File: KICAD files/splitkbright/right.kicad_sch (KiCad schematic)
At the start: 83 parts, among them SW31 SW_Push, SW32 SW_Push, SW37 SW_Push, SW38 SW_Push, SW39 SW_Push, SW40 SW_Push, SW41 SW_Push, SW42 SW_Push, SW43 SW_Push, SW44 SW_Push, SW45 SW_Push, SW46 SW_Push, SW47 SW_Push, SW48 SW_Push, SW49 SW_Push, SW50 SW_Push, SW51 SW_Push, SW52 SW_Push, SW53 SW_Push, SW54 SW_Push, SW55 SW_Push, SW56 SW_Push, SW57 SW_Push, SW58 SW_Push, SW59 SW_Push, SW60 SW_Push, SW61 SW_Push, SW62 SW_Push, SW63 SW_Push, SW64 SW_Push, SW65 SW_Push, SW66 SW_Push, SW67 SW_Push, SW68 SW_Push, SW69 SW_Push, SW70 SW_Push, SW71 SW_Push, SW72 SW_Push, SW73 SW_Push, SW74 SW_Push, U1 nice_nano

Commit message: Edited PCBs
- Added mounting holes to both pcbs and schematics
- Changed the shape and size of both PCBs
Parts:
- added H1, H2, H3, H4: MountingHole, symbol Mechanical:MountingHole
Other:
- note added: "Mounting holes"

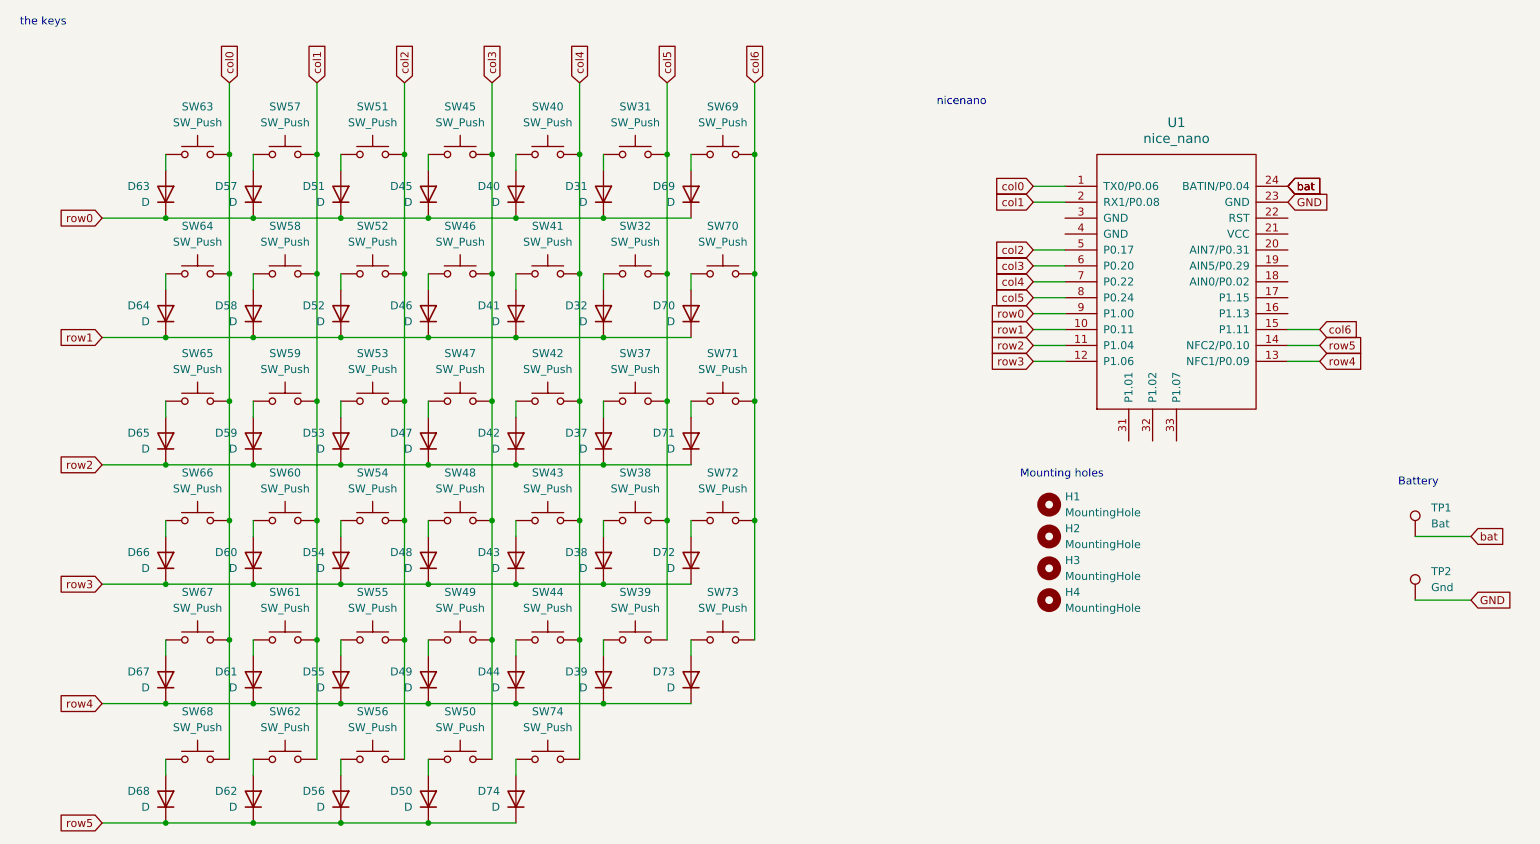
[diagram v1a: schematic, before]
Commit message: Edited PCB.
- Changed the footprint used for the dev board.
- Ran traces again for the dev board.
- Made a custom symbol and footprint for the devboard.
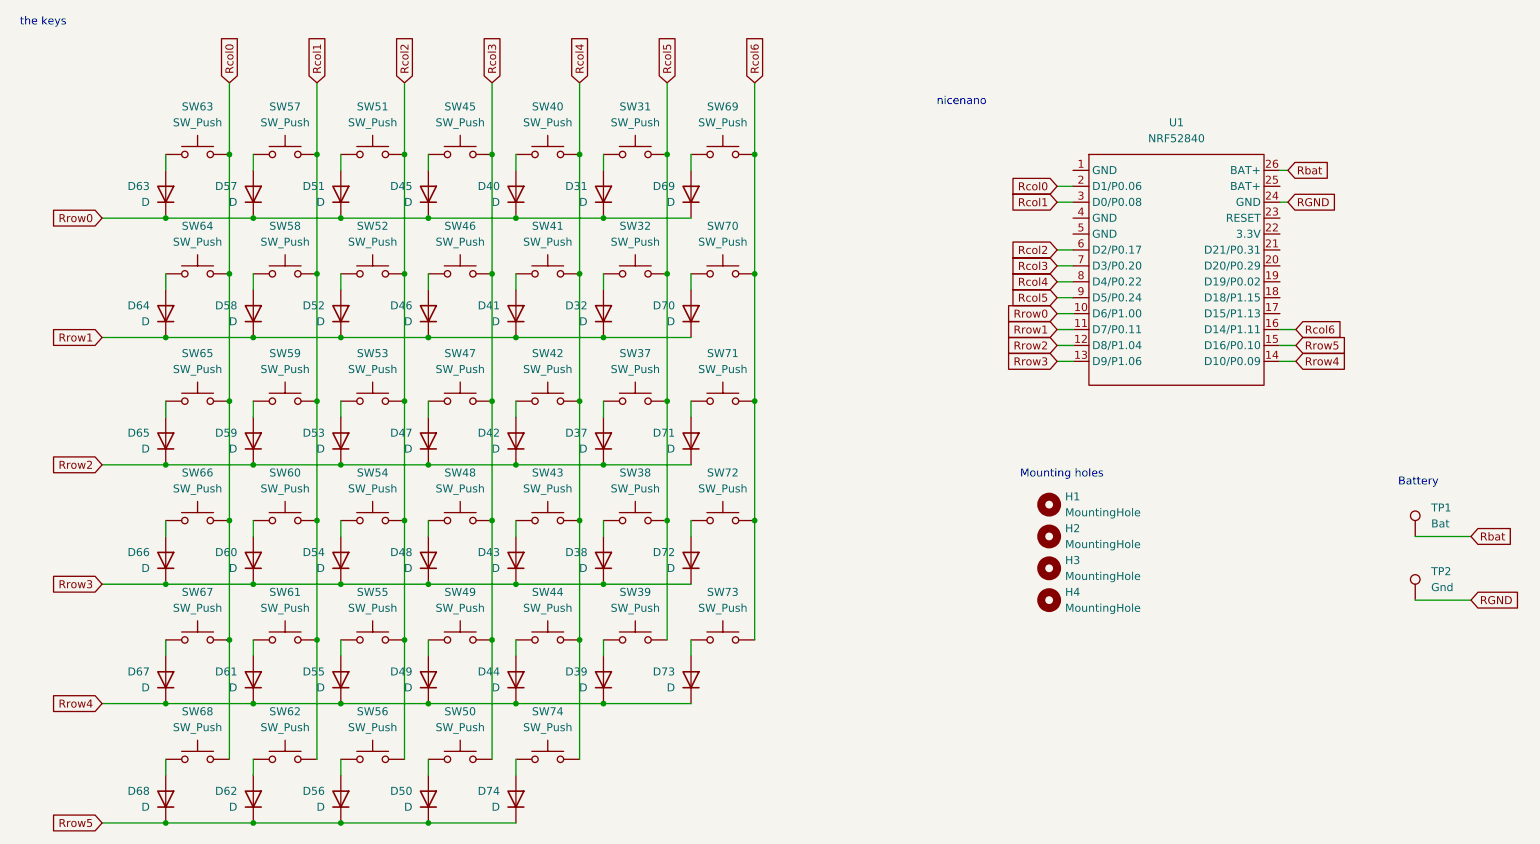
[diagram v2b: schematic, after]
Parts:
- removed U1: nice_nano, nice-nano-kicad-master:nice_nano, symbol nice_nano:nice_nano
- added U1: NRF52840, nice-nano-kicad-master:NRF52840, symbol NRF52840_library:NRF52840
- H1, H2, H3, H4: footprint (none) -> MountingHole:MountingHole_2.2mm_M2
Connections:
- net GND renamed RGND
- net RGND: now also U1.24 (GND)
- net bat renamed Rbat
- net Rbat: now also U1.26 (BAT+)
- net col0 renamed Rcol0
- net Rcol0: now also U1.2 (D1/P0.06)
- net col1 renamed Rcol1
- net Rcol1: now also U1.3 (D0/P0.08)
- net col2 renamed Rcol2
- net Rcol2: now also U1.6 (D2/P0.17)
- net col3 renamed Rcol3
- net Rcol3: now also U1.7 (D3/P0.20)
- net col4 renamed Rcol4
- net Rcol4: now also U1.8 (D4/P0.22)
- net col5 renamed Rcol5
- net Rcol5: now also U1.9 (D5/P0.24)
- net col6 renamed Rcol6
- net Rcol6: now also U1.16 (D14/P1.11)
- net row0 renamed Rrow0
- net Rrow0: now also U1.10 (D6/P1.00)
- net row1 renamed Rrow1
- net Rrow1: now also U1.11 (D7/P0.11)
- net row2 renamed Rrow2
- net Rrow2: now also U1.12 (D8/P1.04)
- net row3 renamed Rrow3
- net Rrow3: now also U1.13 (D9/P1.06)
- net row4 renamed Rrow4
- net Rrow4: now also U1.14 (D10/P0.09)
- net row5 renamed Rrow5
- net Rrow5: now also U1.15 (D16/P0.10)
